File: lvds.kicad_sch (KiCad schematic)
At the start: 105 parts, among them J3 Conn_FFC_Amphenol_62684-40210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, Q2 PJE138K, Q3 SSM3J332R, Q4 PJE138K, Q5 SSM3J332R, Q6 PJE138K, Q7 SSM3J332R, U4 TPS65150PWP, U5 MPQ7235GQBE, U6 TLV76701_WSON6

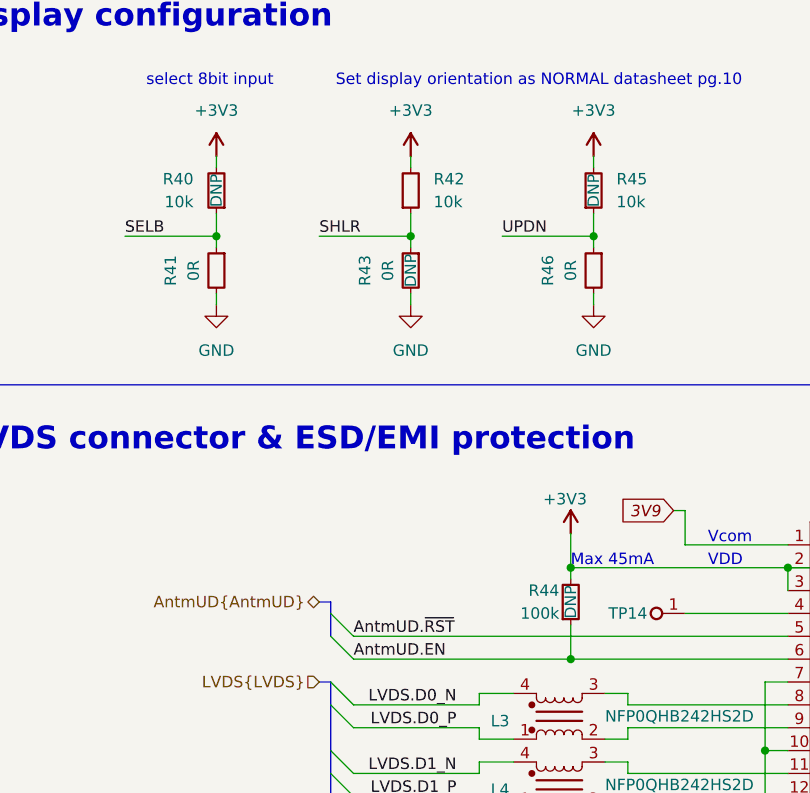
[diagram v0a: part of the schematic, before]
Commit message: [#54932] Sch: clean DNP's
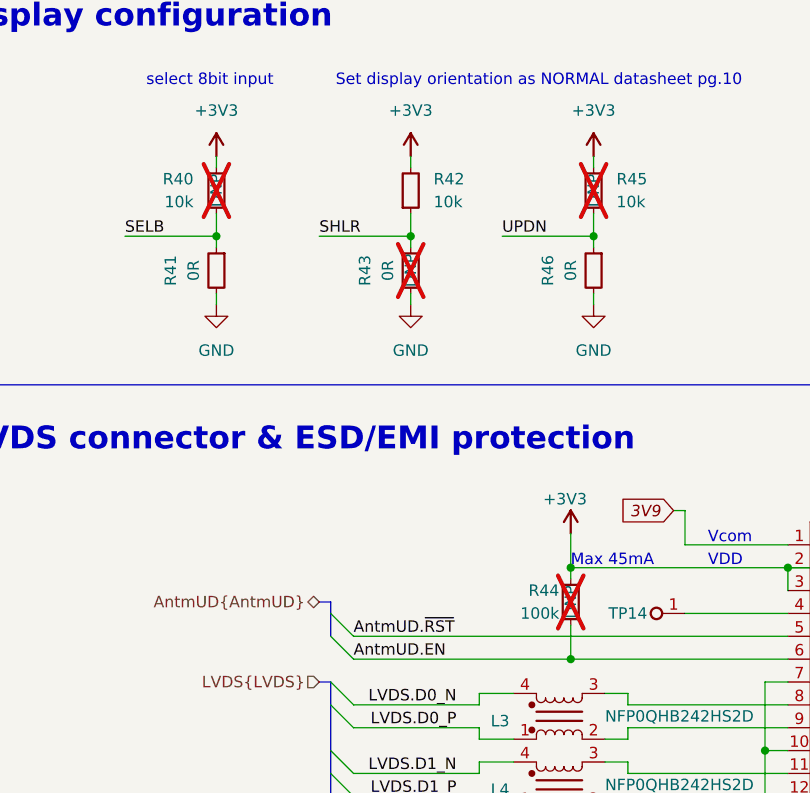
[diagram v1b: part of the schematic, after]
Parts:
- R40, R44, R45: now not fitted; now left out of the parts list
- R43: now not fitted
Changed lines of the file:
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@@
     (effects (font (size 1.27 1.27)) (justify left bottom))
   )
-  (label "AntmUD.~{RST}" (at 345.44 132.08 0)
+  (label "AntmUD.~{RST}" (at 345.44 132.08 0) (fields_autoplaced)
     (effects (font (size 1.27 1.27)) (justify left bottom))
   )
@@
   )
   (symbol (lib_id "antmicroResistors0402:R_10k_0402") (at 372.11 85.09 90) (unit 1)
-    (in_bom yes) (on_board yes) (dnp no)
+    (in_bom no) (on_board yes) (dnp yes)
     (property "Reference" "R45" (at 374.65 81.2799 90)
       (effects (font (size 1.27 1.27) (thickness 0.15)) (justify right))
@@
   )
   (symbol (lib_id "antmicroResistors0402:R_0R_0402") (at 351.79 88.9 270) (unit 1)
-    (in_bom no) (on_board yes) (dnp no)
+    (in_bom no) (on_board yes) (dnp yes)
     (property "Reference" "R43" (at 346.71 91.44 0)
       (effects (font (size 1.27 1.27) (thickness 0.15)))
@@
   )
   (symbol (lib_id "antmicroResistors0402:R_100k_0402") (at 369.57 130.81 90) (unit 1)
-    (in_bom yes) (on_board yes) (dnp no)
+    (in_bom no) (on_board yes) (dnp yes)
     (property "Reference" "R44" (at 368.3 127 90)
       (effects (font (size 1.27 1.27) (thickness 0.15)) (justify left))
@@
   )
   (symbol (lib_id "antmicroResistors0402:R_10k_0402") (at 330.2 85.09 270) (mirror x) (unit 1)
-    (in_bom yes) (on_board yes) (dnp no)
+    (in_bom no) (on_board yes) (dnp yes)
     (property "Reference" "R40" (at 327.66 81.2799 90)
       (effects (font (size 1.27 1.27) (thickness 0.15)) (justify right))

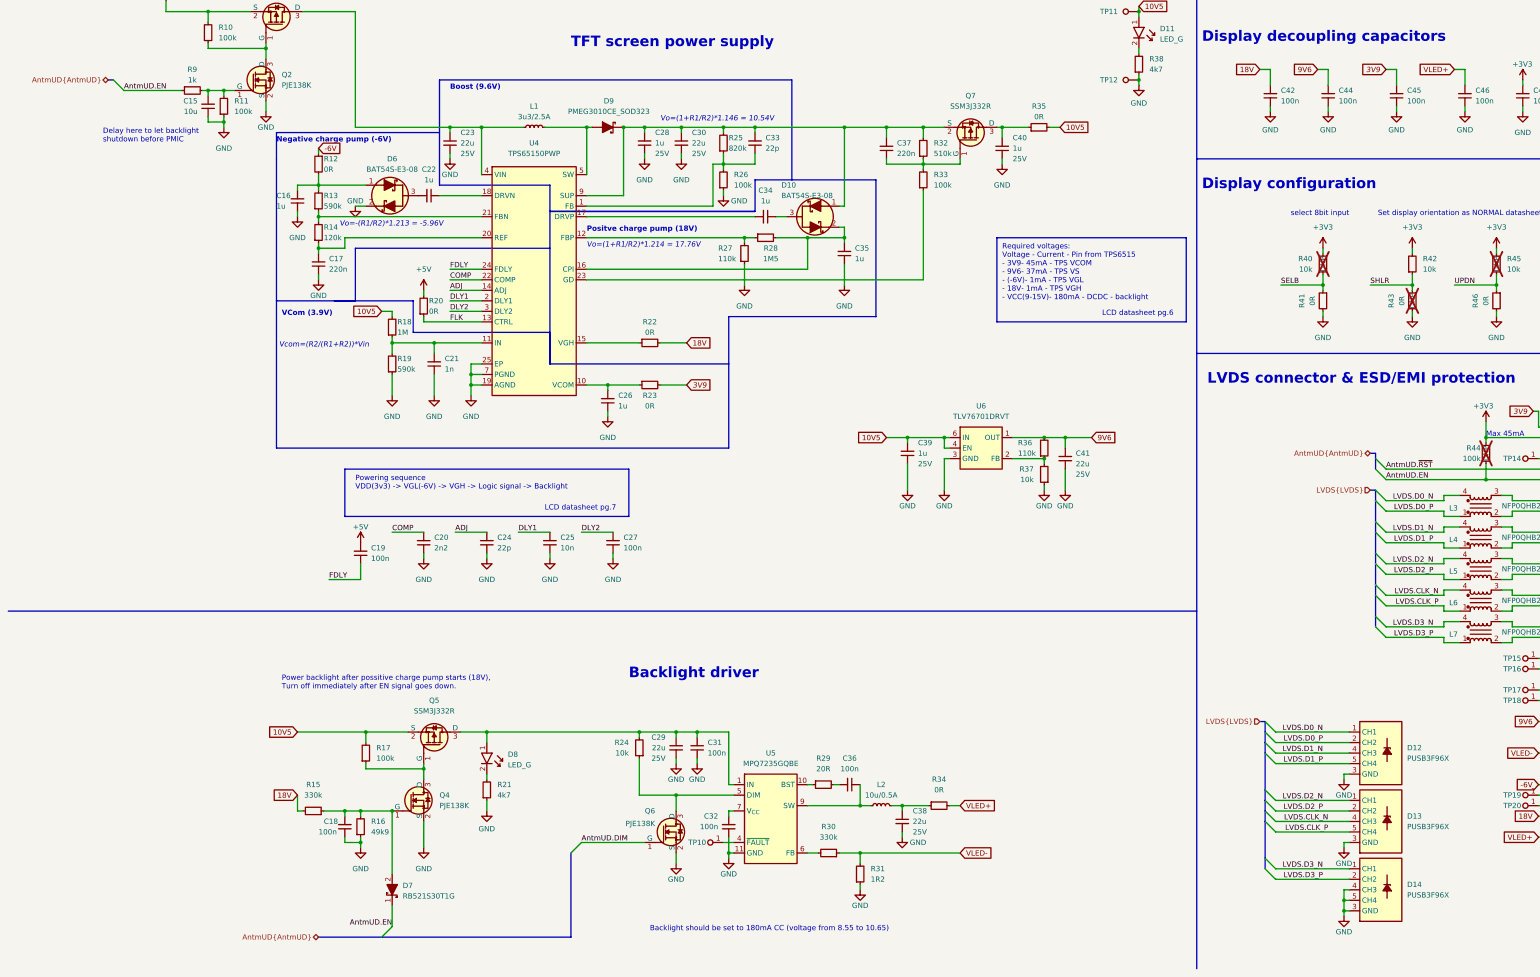
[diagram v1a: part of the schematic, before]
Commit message: [#54932] Sch: update net labels
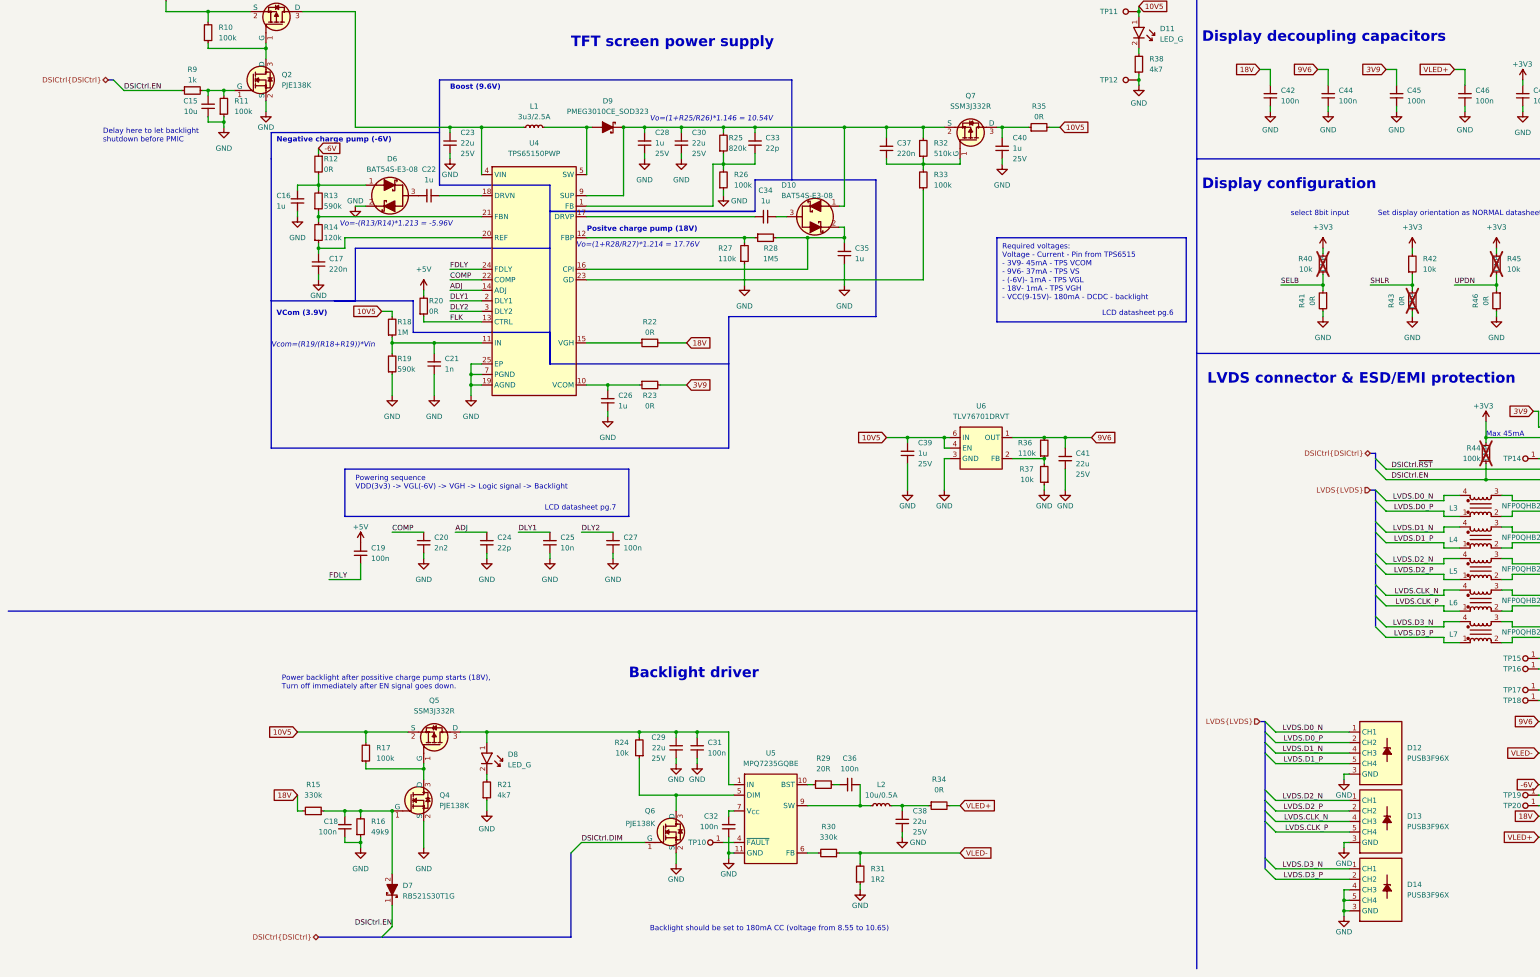
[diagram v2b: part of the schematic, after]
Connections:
- net AntmUD.DIM renamed DSICtrl.DIM
- net AntmUD.EN renamed DSICtrl.EN
- net AntmUD.~{RST} renamed DSICtrl.~{RST}
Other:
- note added: "Vcom=(R19/(R18+R19))*Vin"
- note added: "Vo=(1+R25/R26)*1.146 = 10.54V"
- note added: "Vo=(1+R28/R27)*1.214 = 17.76V"
- note added: "Vo=-(R13/R14)*1.213 = -5.96V"
- note removed: "Vcom=(R2/(R1+R2))*Vin"
- note removed: "Vo=(1+R1/R2)*1.146 = 10.54V"
- note removed: "Vo=(1+R1/R2)*1.214 = 17.76V"
- note removed: "Vo=-(R1/R2)*1.213 = -5.96V"
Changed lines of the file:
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@@
     (stroke (width 0) (type default))
   )
-  (polyline (pts (xy 77.47 50.8) (xy 114.3 50.8))
+  (polyline (pts (xy 76.2 50.8) (xy 114.3 50.8))
     (stroke (width 0) (type default))
   )
@@
     (stroke (width 0) (type default))
   )
-  (polyline (pts (xy 77.47 91.44) (xy 77.47 127))
+  (polyline (pts (xy 76.2 91.44) (xy 76.2 127))
     (stroke (width 0) (type default))
   )
@@
     (stroke (width 0) (type default))
   )
-  (polyline (pts (xy 96.52 91.44) (xy 77.47 91.44))
+  (polyline (pts (xy 96.52 91.44) (xy 76.2 91.44))
     (stroke (width 0) (type default))
   )
@@
     (stroke (width 0) (type default))
   )
-  (polyline (pts (xy 77.47 127) (xy 186.69 127))
+  (polyline (pts (xy 76.2 127) (xy 186.69 127))
     (stroke (width 0) (type default))
   )
@@
     (stroke (width 0) (type default))
   )
-  (polyline (pts (xy 77.47 91.44) (xy 77.47 57.15))
+  (polyline (pts (xy 76.2 91.44) (xy 76.2 57.15))
     (stroke (width 0) (type default))
   )
@@
     (stroke (width 0) (type default))
   )
-  (polyline (pts (xy 77.47 57.15) (xy 77.47 50.8))
+  (polyline (pts (xy 76.2 57.15) (xy 76.2 50.8))
     (stroke (width 0) (type default))
   )
@@
     )
   )
-  (text "Vcom=(R2/(R1+R2))*Vin" (at 78.105 102.87 0)
+  (text "Vcom=(R19/(R18+R19))*Vin" (at 76.2 102.87 0)
     (effects (font (size 1.27 1.27) italic) (justify left bottom))
   )
@@
     (effects (font (size 1.27 1.27) bold) (justify left bottom))
   )
-  (text "VCom (3.9V)" (at 78.74 95.25 0)
+  (text "VCom (3.9V)" (at 77.47 95.25 0)
     (effects (font (size 1.27 1.27) bold) (justify left bottom))
   )
@@
     (effects (font (size 1.27 1.27)) (justify left bottom))
   )
-  (text "Vo=(1+R1/R2)*1.146 = 10.54V\n" (at 170.18 48.26 0)
+  (text "Vo=(1+R25/R26)*1.146 = 10.54V\n" (at 167.64 48.26 0)
     (effects (font (size 1.27 1.27) italic) (justify left bottom))
   )
@@
     (effects (font (size 2.54 2.54) (thickness 0.508) bold) (justify left bottom))
   )
-  (text "Vo=-(R1/R2)*1.213 = -5.96V" (at 92.71 73.66 0)
+  (text "Vo=-(R13/R14)*1.213 = -5.96V" (at 92.71 73.66 0)
     (effects (font (size 1.27 1.27) italic) (justify left bottom))
   )
@@
     (effects (font (size 2.54 2.54) (thickness 0.508) bold) (justify left bottom))
   )
-  (text "Vo=(1+R1/R2)*1.214 = 17.76V" (at 152.4 78.74 0)
+  (text "Vo=(1+R28/R27)*1.214 = 17.76V" (at 149.86 78.74 0)
     (effects (font (size 1.27 1.27) italic) (justify left bottom))
   )
@@
     (effects (font (size 1.27 1.27)) (justify left bottom))
   )
-  (label "AntmUD.~{RST}" (at 345.44 132.08 0) (fields_autoplaced)
+  (label "DSICtrl.~{RST}" (at 346.71 132.08 0) (fields_autoplaced)
     (effects (font (size 1.27 1.27)) (justify left bottom))
   )
-  (label "AntmUD.DIM" (at 151.13 222.25 0) (fields_autoplaced)
+  (label "DSICtrl.DIM" (at 151.13 222.25 0) (fields_autoplaced)
     (effects (font (size 1.27 1.27)) (justify left bottom))
   )
-  (label "AntmUD.EN" (at 345.44 134.62 0) (fields_autoplaced)
+  (label "DSICtrl.EN" (at 346.71 134.62 0) (fields_autoplaced)
     (effects (font (size 1.27 1.27)) (justify left bottom))
   )
@@
     (effects (font (size 1.27 1.27)) (justify left bottom))
   )
-  (label "AntmUD.EN" (at 105.41 242.57 180) (fields_autoplaced)
+  (label "DSICtrl.EN" (at 105.41 242.57 180) (fields_autoplaced)
     (effects (font (size 1.27 1.27)) (justify right bottom))
   )
@@
     (effects (font (size 1.27 1.27)) (justify right bottom))
   )
-  (label "AntmUD.EN" (at 40.64 40.64 0) (fields_autoplaced)
+  (label "DSICtrl.EN" (at 40.64 40.64 0) (fields_autoplaced)
     (effects (font (size 1.27 1.27)) (justify left bottom))
   )
@@
     )
   )
-  (hierarchical_label "AntmUD{AntmUD}" (shape bidirectional) (at 36.83 38.1 180) (fields_autoplaced)
+  (hierarchical_label "DSICtrl{DSICtrl}" (shape bidirectional) (at 36.83 38.1 180) (fields_autoplaced)
     (effects (font (size 1.27 1.27)) (justify right))
   )
-  (hierarchical_label "AntmUD{AntmUD}" (shape bidirectional) (at 341.63 128.27 180) (fields_autoplaced)
+  (hierarchical_label "DSICtrl{DSICtrl}" (shape bidirectional) (at 341.63 128.27 180) (fields_autoplaced)
     (effects (font (size 1.27 1.27)) (justify right))
   )
-  (hierarchical_label "AntmUD{AntmUD}" (shape bidirectional) (at 87.63 245.11 180) (fields_autoplaced)
+  (hierarchical_label "DSICtrl{DSICtrl}" (shape bidirectional) (at 87.63 245.11 180) (fields_autoplaced)
     (effects (font (size 1.27 1.27)) (justify right))
   )
@@
   )
   (symbol (lib_id "antmicroDiodesRectifiersSingle:PMEG3010CE_SOD323") (at 153.67 49.53 0) (unit 1)
-    (in_bom yes) (on_board yes) (dnp no) (fields_autoplaced)
-    (property "Reference" "D9" (at 157.734 43.18 0)
+    (in_bom yes) (on_board yes) (dnp no)
+    (property "Reference" "D9" (at 157.48 43.18 0)
       (effects (font (size 1.27 1.27) (thickness 0.15)))
     )
-    (property "Value" "PMEG3010CE_SOD323" (at 157.734 45.72 0)
+    (property "Value" "PMEG3010CE_SOD323" (at 157.48 45.72 0)
       (effects (font (size 1.27 1.27) (thickness 0.15)))
     )
